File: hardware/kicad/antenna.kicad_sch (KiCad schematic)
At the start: 13 parts, among them J5 BWIPX-1-001E

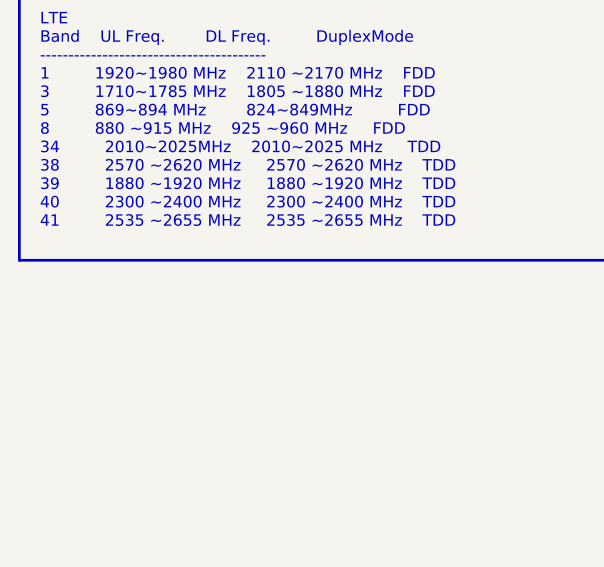
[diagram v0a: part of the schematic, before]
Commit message: add freq info
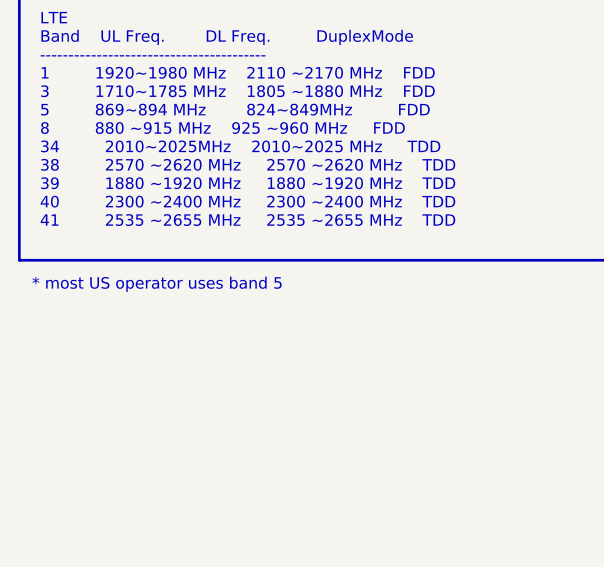
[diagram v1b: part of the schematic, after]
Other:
- note added: "* most US operator uses band 5"
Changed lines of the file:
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@@
     (effects (font (size 2 2) (thickness 0.6) bold) (justify left bottom))
+  )
+  (text "* most US operator uses band 5" (at 15.748 69.088 0)
+    (effects (font (size 1.27 1.27)) (justify left bottom))
   )
   (text "Use Skyworks Solutions SKY13416-485LF for RF Switch"

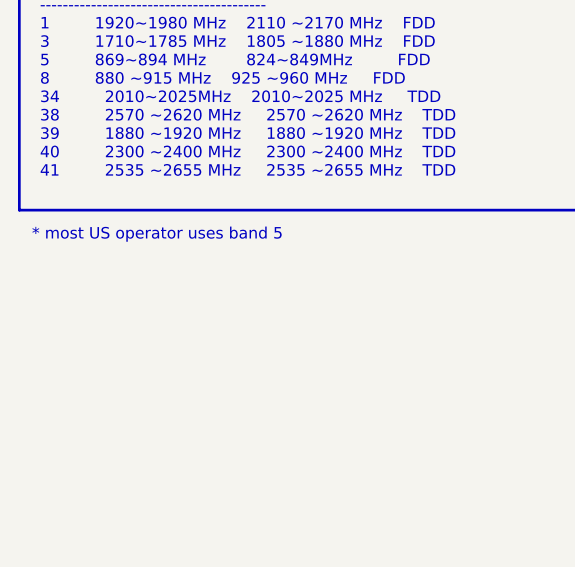
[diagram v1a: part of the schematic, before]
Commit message: add freq info
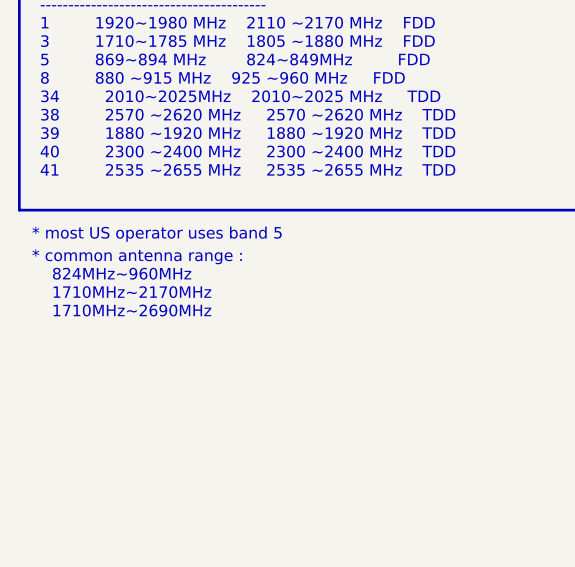
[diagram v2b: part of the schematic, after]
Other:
- note added: "* common antenna range : 824MHz~960MHz 1710MHz~2170MHz 1710MHz~2690MHz"
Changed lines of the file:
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@@
+    (effects (font (size 1.27 1.27)) (justify left bottom))
+  )
+  (text "* common antenna range :\n	824MHz~960MHz\n	1710MHz~2170MHz \n	1710MHz~2690MHz"
+    (at 15.748 77.724 0)
     (effects (font (size 1.27 1.27)) (justify left bottom))
   )

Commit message: update freq
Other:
- note added: "2G DL UL ----------------------------- EGSM900 925~960 MHz 880~915 MHz DCS1800 1805~1880 MHz 1710~1785 MHz LTE Band UL Freq. DL Freq. DuplexMode ---------------------------------------- 1 1920~1980 MHz 2110~2170 MHz FDD 3 1710~1785 MHz 1805~1880 MHz FDD 5 869~894 MHz 824~849 MHz FDD 8 880~915 MHz 925~960 MHz FDD 34 2010~2025 MHz 2010~2025 MHz TDD 38 2570~2620 MHz 2570~2620 MHz TDD 39 1880~1920 MH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"
- note removed: "2G DL UL ----------------------------- EGSM900 925~960MHz 880~915 MHz DCS1800 1805~1880 MHz 1710~1785 MHz LTE Band UL Freq. DL Freq. DuplexMode ---------------------------------------- 1 1920~1980 MHz 2110 ~2170 MHz FDD 3 1710~1785 MHz 1805 ~1880 MHz FDD 5 869~894 MHz 824~849MHz FDD 8 880 ~915 MHz 925 ~960 MHz FDD 34 2010~2025MHz 2010~2025 MHz TDD 38 2570 ~2620 MHz 2570 ~2620 MHz TDD 39 1880 ~192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"
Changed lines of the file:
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@@
     (effects (font (size 1.27 1.27)) (justify left bottom))
   )
-  (text "2G		DL				UL\n-----------------------------\nEGSM900	925~960MHz 		880~915 MHz\nDCS1800	1805~1880 MHz 	1710~1785 MHz\n\nLTE\nBand	UL Freq.		DL Freq. 		DuplexMode\n----------------------------------------\n1 		1920~1980 MHz	2110 ~2170 MHz	FDD\n3 		1710~1785 MHz	1805 ~1880 MHz	FDD\n5 		869~894 MHz		824~849MHz 		FDD\n8 		880 ~915 MHz	925 ~960 MHz 	FDD\n34 		2010~2025MHz	2010~2025 MHz 	TDD\n38 		2570 ~2620 MHz 	2570 ~2620 MHz	TDD\n39 		1880 ~1920 MHz 	1880 ~1920 MHz	TDD\n40 		2300 ~2400 MHz 	2300 ~2400 MHz	TDD\n41 		2535 ~2655 MHz 	2535 ~2655 MHz	TDD"
+  (text "2G		DL				UL\n-----------------------------\nEGSM900	  925~960 MHz	  880~915 MHz\nDCS1800	1805~1880 MHz 	1710~1785 MHz\n\nLTE\nBand	UL Freq.		DL Freq. 		DuplexMode\n----------------------------------------\n1 		1920~1980 MHz	2110~2170 MHz	FDD\n3 		1710~1785 MHz	1805~1880 MHz	FDD\n5 		  869~894 MHz	  824~849 MHz	FDD\n8 		  880~915 MHz	  925~960 MHz 	FDD\n34 		2010~2025 MHz	2010~2025 MHz 	TDD\n38 		2570~2620 MHz 	2570~2620 MHz	TDD\n39 		1880~1920 MHz 	1880~1920 MHz	TDD\n40 		2300~2400 MHz 	2300~2400 MHz	TDD\n41 		2535~2655 MHz 	2535~2655 MHz	TDD"
     (at 16.637 62.103 0)
     (effects (font (size 1.27 1.27)) (justify left bottom))

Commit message: update antenna
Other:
- note added: "Cell Source Matching Network"
- note added: "GNSS Source Matching Network"
- note removed: "Cell Matching Network"
- note removed: "GNSS Matching Network"
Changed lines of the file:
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@@
     (fill (type none))
   )
-  (text "Cell Matching Network" (at 169.926 84.201 0)
+  (text "Cell Source Matching Network" (at 157.607 84.963 0)
     (effects (font (size 2 2) (thickness 0.6) bold) (justify left bottom))
   )
@@
     (effects (font (size 1.27 1.27)) (justify left bottom))
   )
-  (text "GNSS Matching Network" (at 167.386 115.824 0)
+  (text "GNSS Source Matching Network" (at 155.956 116.586 0)
     (effects (font (size 2 2) (thickness 0.6) bold) (justify left bottom))
   )

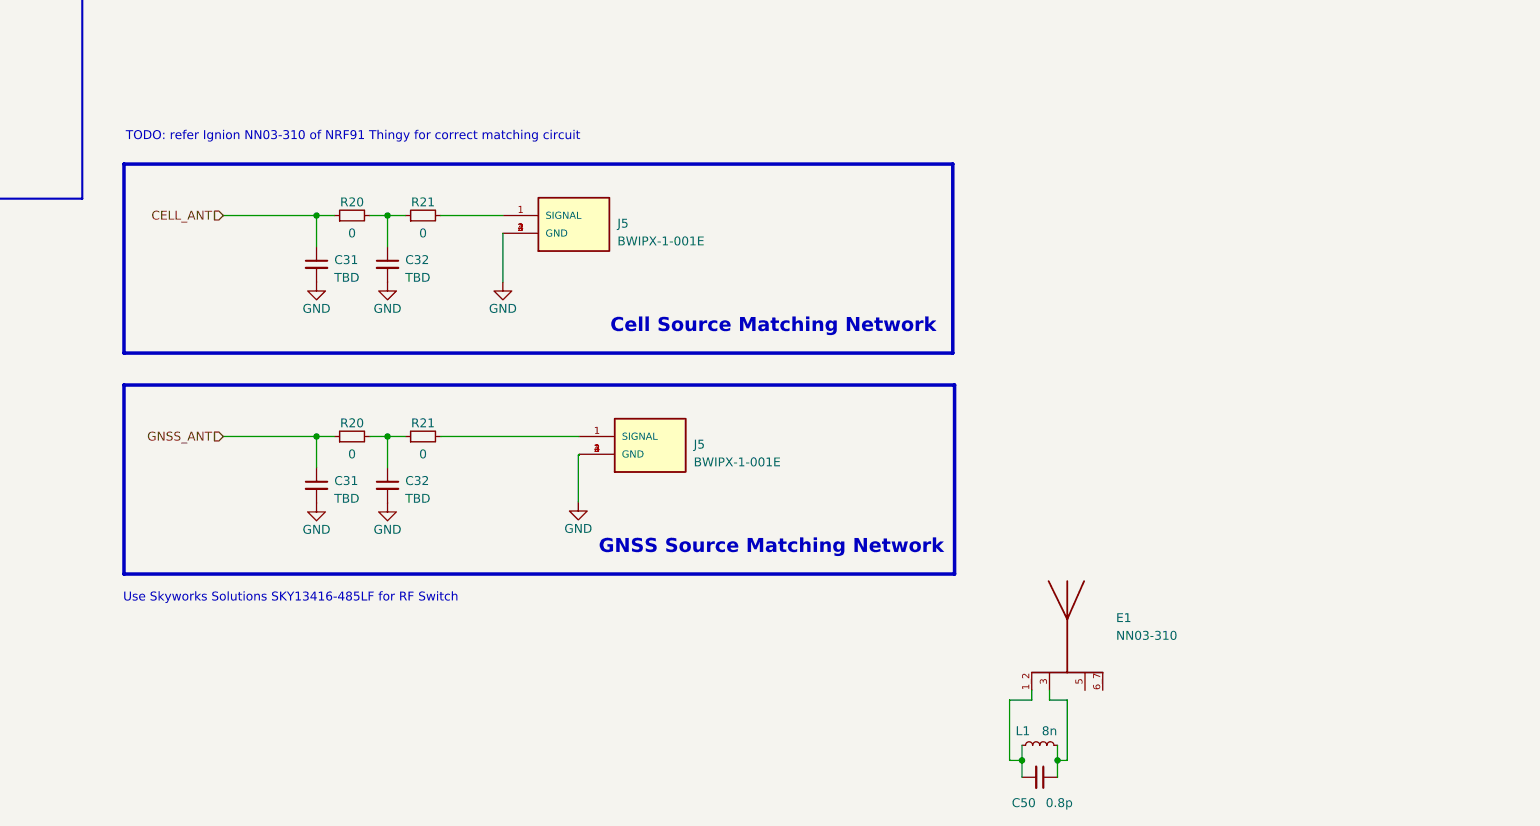
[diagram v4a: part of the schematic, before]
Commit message: update antenna design
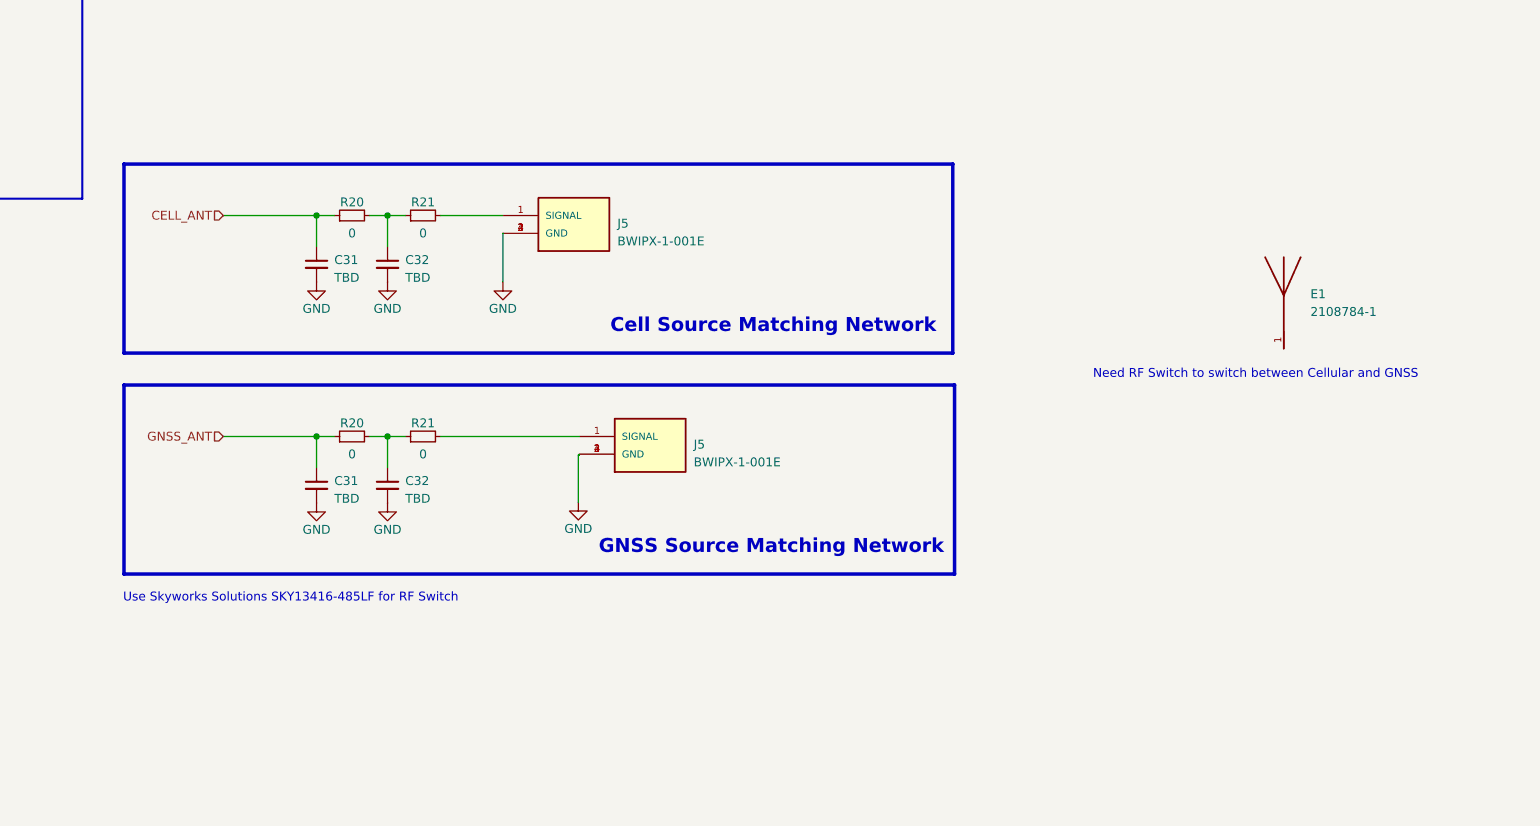
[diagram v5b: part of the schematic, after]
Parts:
- removed C50: 0.8p, symbol Device:C_Small
- removed E1: NN03-310, bwlc1a:NN03-310, symbol bwlc1a:NN03-310
- removed L1: 8n, symbol Device:L_Small
- added E1: 2108784-1, bwlc1a:2108784-1, symbol bwlc1a:2108784-1
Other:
- note added: "Need RF Switch to switch between Cellular and GNSS"
- note removed: "TODO: refer Ignion NN03-310 of NRF91 Thingy for correct matching circuit"
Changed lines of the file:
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@@
 (kicad_sch (version 20230121) (generator eeschema)
   (paper "A4")
-  (junction (at 221.615 145.923) (diameter 0) (color 0 0 0 0)
-  )
   (junction (at 125.73 99.568) (diameter 0) (color 0 0 0 0)
   )
@@
   (junction (at 115.57 99.568) (diameter 0) (color 0 0 0 0)
   )
-  (junction (at 216.535 145.923) (diameter 0) (color 0 0 0 0)
-  )
   (junction (at 115.57 67.945) (diameter 0) (color 0 0 0 0)
   )
@@
     (stroke (width 0) (type default))
   )
-  (wire (pts (xy 221.615 145.923) (xy 221.615 148.336))
-    (stroke (width 0) (type default))
-  )
-  (wire (pts (xy 221.615 143.764) (xy 221.615 145.923))
-    (stroke (width 0) (type default))
-  )
   (wire (pts (xy 142.24 70.485) (xy 142.24 77.47))
     (stroke (width 0) (type default))
   )
-  (wire (pts (xy 223.012 145.923) (xy 223.012 137.287))
-    (stroke (width 0) (type default))
-  )
   (wire (pts (xy 115.57 99.568) (xy 115.57 104.013))
     (stroke (width 0) (type default))
@@
     (stroke (width 0) (type default))
   )
-  (wire (pts (xy 217.932 137.287) (xy 214.757 137.287))
-    (stroke (width 0) (type default))
-  )
-  (wire (pts (xy 216.535 143.764) (xy 216.535 145.923))
-    (stroke (width 0) (type default))
-  )
   (wire (pts (xy 153.162 102.235) (xy 153.035 102.235))
     (stroke (width 0) (type default))
   )
-  (wire (pts (xy 223.012 137.287) (xy 220.472 137.287))
-    (stroke (width 0) (type default))
-  )
-  (wire (pts (xy 214.757 145.923) (xy 216.535 145.923))
-    (stroke (width 0) (type default))
-  )
-  (wire (pts (xy 220.472 137.287) (xy 220.472 135.89))
-    (stroke (width 0) (type default))
-  )
   (wire (pts (xy 153.035 102.235) (xy 153.035 108.966))
     (stroke (width 0) (type default))
   )
-  (wire (pts (xy 216.535 145.923) (xy 216.535 148.336))
-    (stroke (width 0) (type default))
-  )
-  (wire (pts (xy 214.757 137.287) (xy 214.757 145.923))
-    (stroke (width 0) (type default))
-  )
   (wire (pts (xy 125.73 99.568) (xy 125.73 104.013))
     (stroke (width 0) (type default))
   )
-  (wire (pts (xy 217.932 135.89) (xy 217.932 137.287))
-    (stroke (width 0) (type default))
-  )
   (wire (pts (xy 123.19 99.568) (xy 125.73 99.568))
-    (stroke (width 0) (type default))
-  )
-  (wire (pts (xy 221.615 145.923) (xy 223.012 145.923))
     (stroke (width 0) (type default))
   )
@@
     (effects (font (size 2 2) (thickness 0.4) bold) (justify left bottom))
   )
-  (text "TODO: refer Ignion NN03-310 of NRF91 Thingy for correct matching circuit"
-    (at 88.265 57.404 0)
+  (text "Need RF Switch to switch between Cellular and GNSS"
+    (at 226.695 91.44 0)
     (effects (font (size 1.27 1.27)) (justify left bottom))
   )
@@
     )
   )
-  (symbol (lib_id "Device:L_Small") (at 219.075 143.764 90) (unit 1)
-    (in_bom yes) (on_board yes) (dnp no)
-    (property "Reference" "L1" (at 216.662 141.732 90)
-      (effects (font (size 1.27 1.27)))
-    )
-    (property "Value" "8n" (at 220.472 141.732 90)
-      (effects (font (size 1.27 1.27)))
-    )
-    (property "Footprint" "" (at 219.075 143.764 0)
-      (effects (font (size 1.27 1.27)) hide)
-    )
-    (property "Datasheet" "~" (at 219.075 143.764 0)
-      (effects (font (size 1.27 1.27)) hide)
-    )
-    (pin "1")
-    (pin "2")
-    (instances
-      (project "bwlc1a"
-        (path "/388039b1-99cc-430f-bd4a-010573fde798/ca79f09e-abdb-462a-9aab-98f2e37e5b23"
-          (reference "L1") (unit 1)
+  (symbol (lib_id "bwlc1a:2108784-1") (at 254 81.915 0) (unit 1)
+    (in_bom yes) (on_board yes) (dnp no) (fields_autoplaced)
+    (property "Reference" "E1" (at 257.81 79.1845 0)
+      (effects (font (size 1.27 1.27)) (justify left))
+    )
+    (property "Value" "2108784-1" (at 257.81 81.7245 0)
+      (effects (font (size 1.27 1.27)) (justify left))
+    )
+    (property "Footprint" "bwlc1a:2108784-1" (at 254 81.915 0)
+      (effects (font (size 1.27 1.27)) (justify bottom) hide)
+    )
+    (property "Datasheet" "" (at 254 81.915 0)
+      (effects (font (size 1.27 1.27)) hide)
+    )
+    (pin "1")
+    (instances
+      (project "bwlc1a"
+        (path "/388039b1-99cc-430f-bd4a-010573fde798/ca79f09e-abdb-462a-9aab-98f2e37e5b23"
+          (reference "E1") (unit 1)
         )
       )
@@
         (path "/388039b1-99cc-430f-bd4a-010573fde798/ca79f09e-abdb-462a-9aab-98f2e37e5b23"
           (reference "#PWR072") (unit 1)
-        )
-      )
-    )
-  )
-  (symbol (lib_id "bwlc1a:NN03-310") (at 223.012 128.27 0) (unit 1)
-    (in_bom yes) (on_board yes) (dnp no) (fields_autoplaced)
-    (property "Reference" "E1" (at 229.997 125.5395 0)
-      (effects (font (size 1.27 1.27)) (justify left))
-    )
-    (property "Value" "NN03-310" (at 229.997 128.0795 0)
-      (effects (font (size 1.27 1.27)) (justify left))
-    )
-    (property "Footprint" "bwlc1a:NN03-310" (at 223.012 143.51 0)
-      (effects (font (size 1.27 1.27)) (justify bottom) hide)
-    )
-    (property "Datasheet" "" (at 223.012 128.27 0)
-      (effects (font (size 1.27 1.27)) hide)
-    )
-    (property "Part Description" "" (at 223.012 128.27 0)
-      (effects (font (size 1.27 1.27)) hide)
-    )
-    (property "Manufacturer" "" (at 223.012 128.27 0)
-      (effects (font (size 1.27 1.27)) hide)
-    )
-    (property "Manufacturer Part Number" "" (at 223.012 128.27 0)
-      (effects (font (size 1.27 1.27)) hide)
-    )
-    (property "Distributor" "" (at 223.012 128.27 0)
-      (effects (font (size 1.27 1.27)) hide)
-    )
-    (property "Distributor Part Number" "" (at 223.012 128.27 0)
-      (effects (font (size 1.27 1.27)) hide)
-    )
-    (property "Distributor Link" "" (at 223.012 128.27 0)
-      (effects (font (size 1.27 1.27)) hide)
-    )
-    (pin "1_2")
-    (pin "3")
-    (pin "5")
-    (pin "6_7")
-    (instances
-      (project "bwlc1a"
-        (path "/388039b1-99cc-430f-bd4a-010573fde798/ca79f09e-abdb-462a-9aab-98f2e37e5b23"
-          (reference "E1") (unit 1)
         )
       )
@@
         )
       )
-    )
-  )
-  (symbol (lib_id "Device:C_Small") (at 219.075 148.336 270) (mirror x) (unit 1)
-    (in_bom yes) (on_board yes) (dnp no)
-    (property "Reference" "C50" (at 216.789 152.019 90)
-      (effects (font (size 1.27 1.27)))
-    )
-    (property "Value" "0.8p" (at 221.869 152.019 90)
-      (effects (font (size 1.27 1.27)))
-    )
-    (property "Footprint" "" (at 219.075 148.336 0)
-      (effects (font (size 1.27 1.27)) hide)
-    )
-    (property "Datasheet" "~" (at 219.075 148.336 0)
-      (effects (font (size 1.27 1.27)) hide)
-    )
-    (pin "1")
-    (pin "2")
-    (instances
-      (project "bwlc1a"
-        (path "/388039b1-99cc-430f-bd4a-010573fde798/ca79f09e-abdb-462a-9aab-98f2e37e5b23"
-          (reference "C50") (unit 1)
-        )
-      )
